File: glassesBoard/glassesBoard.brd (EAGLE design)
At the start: 87 x 27.6 mm, 26 parts, among them J1 AXK724147G, J2 105450-0101, U2 APDS-9960, U3 1.8, U4 3.3, U5 SSM3J338RSOT-23F, U6 SSM3J338RSOT-23F, U8 IQS263BDFN10

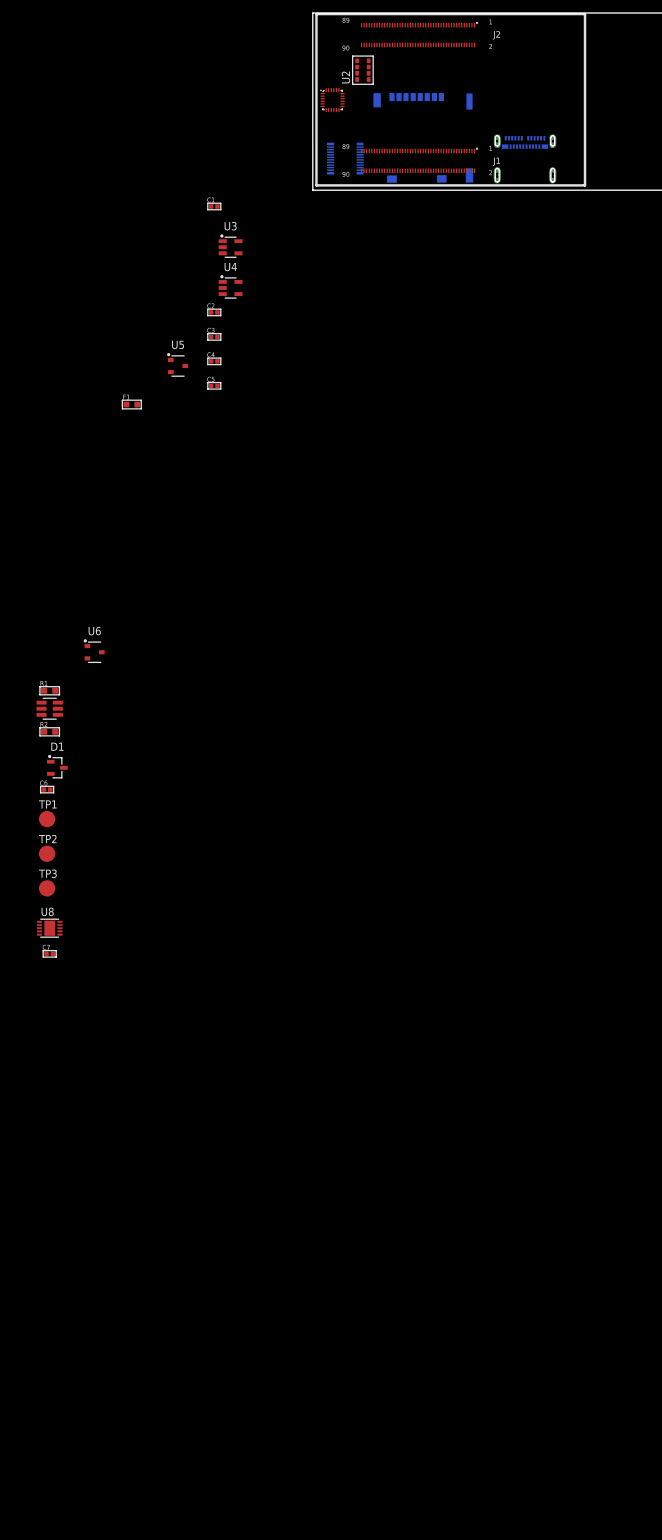
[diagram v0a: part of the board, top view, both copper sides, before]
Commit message: Added display converters and organized schematic
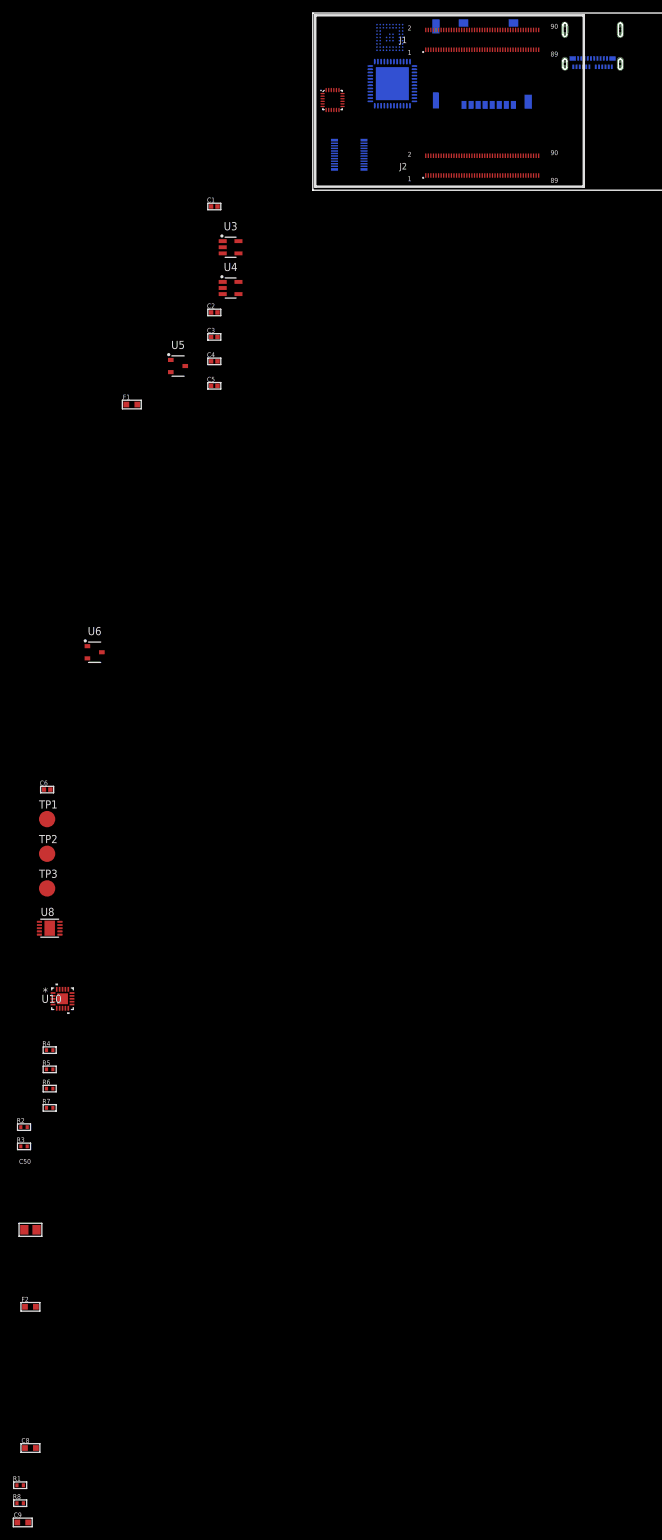
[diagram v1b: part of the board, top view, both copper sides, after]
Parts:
- removed C7: 1uF, thanics-capacitor:C0402
- removed D1: BAS40-06, glasses:SOT23-3
- removed J2: 105450-0101, 105450-0101:MOLEX_105450-0101
- removed U2: APDS-9960, glasses:APDS-9960
- added C50: 22uF, thanics-capacitor:C0805
- added C8, C9: 10uF, thanics-capacitor:C0603
- added F2: SF-0603S200-2, thanics-resistor:R0603
- added J7: 105450-0101, 105450-0101:MOLEX_105450-0101
- added R3: 10k, thanics-resistor:R0402
- added R4: 2.15k, thanics-resistor:R0402
- added R5: 1k, thanics-resistor:R0402
- added R6, R7: 3.2k, thanics-resistor:R0402
- added R8: 56k, thanics-resistor:R0402
- added U10: ATTINY20-MMH, attiny20:20M2
- added U11: SN65LVDS822VQFN48, glasses:QFN50P700X700X100-49T515
- R1: value 10k -> 56k; device 10k-resistor(0603):RC0603N-M -> thanics-resistor:R0402
- R2: device 10k-resistor(0603):RC0603N-M -> thanics-resistor:R0402
- U7: value (none) -> SN65DSI83PBGA-N64; device attiny10:6ST1-M -> glasses:BGA81C50P9X9_500X500X100
- moved R1 123.9 mm to (-36.6, -201.8)
- moved U7 117.3 mm to (21.0, 23.8), flipped to the bottom, turned to 270 degrees
- moved R2 61.7 mm to (-36.0, -146.0)
- moved U$1 22.6 mm to (35.4, 3.87), turned to 180 degrees
- moved U$2 12.4 mm to (37.0, 13.3), turned to 180 degrees
- moved J1 0.85 mm to (14.7, 5.52)
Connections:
- removed net FUSE_SNS: F1.2, R1.2, U6.2
- removed net N$6: C7.1, D1.3, R1.1, U6.1
- removed net SHIELD: J2.P$1, J2.P$2, J2.P$3, J2.P$4, J2.P$5, J2.P$6
- removed net VBUS: J2.A4, J2.A9, J2.B4, J2.B9
- new net !RST: R2.2, TP3.TP, U10.13
- new net !SHUTDOWN_INT: U10.2
- new net +5V: C6.1, C8.1, F2.2, R1.2, R2.1, R8.2, U10.9
- new net ADC: R5.1, R7.2, U10.5
- new net AIN1: R4.1, R6.2, U10.3
- new net FUSED_VBATT: C2.1, F1.2, R3.1, R4.2, R7.1, U3.1, U3.3, U6.2
- new net I2C_SCL_5V: U10.15
- new net I2C_SDA_5V/TPIDATA: TP2.TP, U10.12
- new net N$1: U11.26, U7.C8
- new net N$10: U11.33, U7.G9
- new net N$11: U11.32, U7.F8
- new net N$12: U11.31, U7.F9
- new net N$3: U11.25, U7.C9
- new net N$50: J7.A5, R8.1
- new net N$51: C50.1, F2.1, J7.A4, J7.A9, J7.B4, J7.B9
- new net N$63: J7.B5, R1.1
- new net N$8: U11.29, U7.E9
- new net N$9: U11.34, U7.G8
- new net TPICLK: TP1.TP, U10.11
- net !TOUCH_INT: no longer D1.1
- net +1V8: now also U10.4
- net +3V3: no longer R2.1, U7.5
- net BATT_CNTL: now also R3.2, U10.1, U6.1; no longer D1.2
- net GND: now also C50.2, C6.2, C8.2, J7.A1, J7.A12, J7.B1, J7.B12, J7.P$1, J7.P$2, J7.P$3, J7.P$4, J7.P$5, J7.P$6, R5.2, R6.1, U10.21, U10.8; no longer C7.2, J2.A1, J2.A12, J2.B1, J2.B12, U7.2
- net MIPI_DSI0_CLK_N: now also U7.J5
- net MIPI_DSI0_CLK_P: now also U7.H5
- net MIPI_DSI0_DATA0_N: now also U7.J3
- net MIPI_DSI0_DATA0_P: now also U7.H3
- net MIPI_DSI0_DATA1_N: now also U7.J4
- net MIPI_DSI0_DATA1_P: now also U7.H4
- net MIPI_DSI0_DATA2_N: now also U7.J6
- net MIPI_DSI0_DATA2_P: now also U7.H6
- net MIPI_DSI0_DATA3_N: now also U7.J7
- net MIPI_DSI0_DATA3_P: now also U7.H7
- net N$4: now also U11.28, U7.D8; no longer R2.2, TP1.TP, U7.6
- net N$5: now also U11.27, U7.D9; no longer TP3.TP, U7.3
- net N$7: now also U11.30, U7.E8; no longer TP2.TP, U7.1
- net P$1: no longer C2.1, U3.1, U3.3
- net USB_HS_D_N: now also J7.A7, J7.B7
- net USB_HS_D_P: now also J7.A6, J7.B6

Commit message: Added boot select circuitry
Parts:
- added C7: 22uF, thanics-capacitor:C0805
- added L1: 4.7uH, glasses:1008
- added R10, R11, R14, R15, R16, R9: 10k, thanics-resistor:R0402
- added R12, R13: 5.1k, thanics-resistor:R0603
- added U12: NLAS2750, glasses:UQFN10
- added U13, U15, U9: NX3020NAK, glasses:SOT-23_(TO-236AB)
- added U14: SSM3J338RSOT-23F, glasses:SOTFL95P240X80-3
- added U2: TPS613222A, glasses:SOT23-5
- C9: value 10uF -> 22uF; device thanics-capacitor:C0603 -> thanics-capacitor:C0805
- moved C9 18.4 mm to (-35.8, -226.0)
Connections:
- removed net MIPI_CSI0_CLK_N: U$1.J1.56
- removed net MIPI_CSI0_CLK_P: U$1.J1.58
- removed net MIPI_CSI0_DATA0_N: U$1.J1.64
- removed net MIPI_CSI0_DATA0_P: U$1.J1.66
- removed net MIPI_CSI0_DATA1_N: U$1.J1.60
- removed net MIPI_CSI0_DATA1_P: U$1.J1.62
- removed net MIPI_CSI0_DATA2_N: U$1.J1.48
- removed net MIPI_CSI0_DATA2_P: U$1.J1.50
- removed net MIPI_CSI0_DATA3_N: U$1.J1.52
- removed net MIPI_CSI0_DATA3_P: U$1.J1.54
- removed net N$50: J7.A5, R8.1
- removed net N$63: J7.B5, R1.1
- new net BOOT_CONFIG_0: U$1.J2.24
- new net BOOT_CONFIG_1: U$1.J2.22
- new net BOOT_CONFIG_2: U$1.J2.33
- new net BOOT_CONFIG_3: U$1.J2.26
- new net BOOT_CONFIG_5: R10.1, U$1.J2.35
- new net FORCED_USB_BOOT: U$1.J1.87
- new net I2C0_SCL: U$1.J1.79
- new net I2C0_SDA: U$1.J1.77
- new net I2C2_SCL: U$1.J1.88
- new net I2C2_SDA: U$1.J1.90
- new net I2C3_SCL: U$1.J2.67
- new net I2C3_SDA: U$1.J2.69
- new net MIPI_CSI1_CLK_N: U$1.J1.34
- new net MIPI_CSI1_CLK_P: U$1.J1.36
- new net MIPI_CSI1_DATA0_N: U$1.J1.42
- new net MIPI_CSI1_DATA0_P: U$1.J1.44
- new net MIPI_CSI1_DATA1_N: U$1.J1.38
- new net MIPI_CSI1_DATA1_P: U$1.J1.40
- new net N$13: U10.16, U9.G
- new net N$14: R11.1
- new net N$15: R14.1
- new net N$16: J7.B5, U12.9
- new net N$17: J7.A5, U12.3
- new net N$18: R13.2, U12.10
- new net N$19: R12.2, U12.2
- new net N$20: R1.1, U12.5
- new net N$21: R8.1, U12.7
- new net N$22: R15.2, U12.4, U12.8, U13.S
- new net N$23: R16.1, U14.1, U15.D
- new net N$6: L1.P$1, U2.1
- new net PHONE_ON_N: R9.1, U$1.J2.9, U9.D
- net +1V8: now also R10.2, R11.2, R14.2, R9.2
- net +5V: now also R16.2, U12.1, U13.D, U14.2, U2.4
- net AIN1: now also R6.1; no longer R6.2
- net FUSED_VBATT: now also L1.P$2
- net GND: now also C7.1, C9.2, R12.1, R13.1, R15.1, R6.2, U$1.J1.10, U$1.J1.31, U$1.J1.32, U$1.J1.37, U$1.J1.41, U$1.J1.45, U$1.J1.46, U$1.J1.47, U$1.J1.61, U$1.J1.68, U$1.J1.71, U$1.J1.78, U$1.J1.81, U$1.J1.86, U$1.J2.11, U$1.J2.15, U$1.J2.21, U$1.J2.30, U$1.J2.31, U$1.J2.36, U$1.J2.37, U$1.J2.42, U$1.J2.49, U$1.J2.5, U$1.J2.56, U$1.J2.65, U$1.J2.66, U$1.J2.77, U$1.J2.82, U$1.J2.89, U$1.J2.90, U12.6, U15.S, U2.2, U9.S; no longer R6.1
- net P$1: now also C7.2, C9.1, U$1.J1.1, U$1.J1.2, U$1.J1.3, U$1.J1.4, U$1.J1.5, U$1.J1.6, U$1.J1.7, U$1.J1.8
- net USB_HS_ID: now also U13.G, U15.G
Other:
- board text added: "Touch"

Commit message: Added charger, more boot settings, more power supplies, and fingerprint sensor
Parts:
- removed U$2: MICROSD, glasses:MICROSD
- added C10, C11, C12, C13, C14, C15, C16, C17, C21, C23: 1uF, thanics-capacitor:C0402
- added C18, C19, C20: 100nF, thanics-capacitor:C0402
- added C22: 10uF, thanics-capacitor:C0603
- added J2: DF30FC-30DS-0.4V, thanics-connector:DF30FC-30DS-0.4V
- added R17, R18, R19, R20, R23, R24, R25, R26, R27, R28: 10k, thanics-resistor:R0402
- added R21, R22: 5.1k, thanics-resistor:R0603
- added R29: 2k, thanics-resistor:R0402
- added U16: SSM3J338RSOT-23F, glasses:SOTFL95P240X80-3
- added U17: NX3020NAK, glasses:SOT-23_(TO-236AB)
- added U18: 2.8, glasses:SOT23-5
- added U19: TCR2EF15SOT-25, glasses:SOT95P275X130-5
- added U20: MICROSD, glasses:MICROSD
- added U21: MCP73833, glasses:DFN10-3X3
- J1: value AXK724147G -> BM10NB(0.8)-16DS-0.4V(51); device glasses:P4-24 -> thanics-connector:BM10NB(0.8)-16DS-0.4V(51)
- moved R14 122.0 mm to (-83.0, -359.4)
- moved J1 41.0 mm to (55.2, 12.0), flipped to the top, turned to 0 degrees
- moved U11 4.43 mm to (22.8, 12.4)
- moved U7 3.01 mm to (21.2, 20.8), turned to 180 degrees
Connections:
- new net !FINGER_RST: J1.10, R20.1, U$1.J1.75
- new net CAM1_PWDN: J2.12, U$1.J2.84
- new net CAM1_RST: J2.8, U$1.J1.82
- new net CAM1_XCLK: J2.23, U$1.J1.80
- new net CHARGER_VCC: C23.1, R17.2, U$1.J1.21, U14.3, U21.1, U21.2
- new net CHARGE_STAT1: R27.1, U$1.J2.48, U21.3
- new net CHARGE_STAT2: R28.1, U$1.J2.50, U21.4
- new net DSI_EN: C21.1, R25.2, U7.B1
- new net FINGER_INT: J1.8, U$1.J1.73
- new net N$24: F2.2, R16.2, R19.1, U14.2, U16.3
- new net N$25: R18.2, U16.1, U17.S
- new net N$26: R14.2, U7.A1, U7.H2
- new net N$27: R26.2, U21.8
- new net N$28: R29.2, U21.6
- new net N$29: C20.1, U1.10
- new net PM_RESIN_N: R24.1, U$1.J2.7
- new net SPI0_CLK: J1.16, U$1.J1.63
- new net SPI0_CS: J1.12, U$1.J1.67
- new net SPI0_MISO: J1.11, U$1.J1.69
- new net SPI0_MOSI: J1.15, U$1.J1.65
- net +1V8: now also C11.1, C13.1, C14.1, C17.1, C18.1, C19.1, J1.5, J1.7, J2.10, J2.2, J2.30, J2.6, R20.2, R21.2, R22.2, R24.2, R25.1, R27.2, R28.2, U1.13, U1.22, U1.8, U1.9, U18.5, U19.5, U7.A9, U7.B8, U7.D6, U7.E5, U7.E6, U7.F6, U7.J2; no longer R14.2
- net +3V3: now also C15.2, J1.6
- net +5V: now also U16.2, U17.D; no longer F2.2, R16.2, U14.2
- net GND: now also C10.2, C11.2, C12.2, C13.2, C14.2, C15.1, C16.2, C17.2, C18.2, C19.2, C20.2, C21.2, C22.2, C23.2, J1.13, J1.14, J1.3, J1.4, J1.9, J2.18, J2.21, J2.25, J2.26, J2.27, J2.29, J2.4, R14.1, R17.1, R18.1, R19.2, R23.1, R26.1, R29.1, U1.11, U1.18, U1.20, U18.2, U19.2, U20.10, U20.11, U20.12, U20.13, U20.6, U20.9, U21.5, U21.EXP, U7.A2, U7.A8, U7.B9, U7.D5, U7.E4, U7.F4, U7.F5, U7.H9; no longer U$2.10, U$2.11, U$2.12, U$2.13, U$2.6, U$2.9
- net I2C0_SCL: now also R22.1, U1.23
- net I2C0_SDA: now also R21.1, U1.24
- net I2C2_SCL: now also J2.14
- net I2C2_SDA: now also J2.16
- net I2C3_SCL: now also U7.H1
- net I2C3_SDA: now also U7.J1
- net MIPI_CSI1_CLK_N: now also J2.13
- net MIPI_CSI1_CLK_P: now also J2.15
- net MIPI_CSI1_DATA0_N: now also J2.9
- net MIPI_CSI1_DATA0_P: now also J2.11
- net MIPI_CSI1_DATA1_N: now also J2.17
- net MIPI_CSI1_DATA1_P: now also J2.19
- net N$15: now also C16.1, U7.J8; no longer R14.1
- net P$1: now also C10.1, C12.1, U$1.J1.11, U$1.J1.9, U18.1, U18.3, U19.1, U19.3
- net SDC2_CLK: now also U20.5; no longer U$2.5
- net SDC2_CMD: now also U20.3; no longer U$2.3
- net SDC2_DATA_0: now also U20.7; no longer U$2.7
- net SDC2_DATA_1: now also U20.8; no longer U$2.8
- net SDC2_DATA_2: now also U20.1; no longer U$2.1
- net SDC2_DATA_3: now also U20.2; no longer U$2.2
- net USB_HS_ID: now also R23.2, U17.G
- net VBATT_IN: now also C22.1, U21.10, U21.9
- net VREG_L11_SDC: now also U20.4; no longer U$2.4

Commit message: Started PCB component placement, made a premium service DRC
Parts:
- added C24: 1uF, thanics-capacitor:C0402
- added J3: S2B-XH-A(LF)(SN), thanics-connector:S2B-XH-A(LF)(SN)
- added R30, R31, R32, R33: 5.1k, thanics-resistor:R0402
- R12, R13, R21, R22: device thanics-resistor:R0603 -> thanics-resistor:R0402
- moved C22 421.6 mm to (82.3, 6.16)
- moved R29 421.6 mm to (78.8, 1.93)
- moved C23 420.3 mm to (75.3, 4.77), turned to 270 degrees
- moved R28 412.4 mm to (76.1, 1.67), turned to 270 degrees
- moved R26 412.2 mm to (81.8, 4.65), turned to 180 degrees
- moved R27 409.3 mm to (74.7, 1.67), turned to 270 degrees
- moved U21 407.3 mm to (78.3, 4.36)
- moved C21 403.2 mm to (13.9, 26.4), flipped to the bottom
- moved R25 399.3 mm to (13.9, 25.2), flipped to the bottom, turned to 180 degrees
- moved R14 395.5 mm to (13.9, 24.0), flipped to the bottom, turned to 180 degrees
- moved C17 391.0 mm to (14.3, 22.1), flipped to the bottom, turned to 90 degrees
- moved C16 389.5 mm to (21.9, 21.3), flipped to the bottom, turned to 180 degrees
- moved R23 387.0 mm to (51.5, 11.8), turned to 270 degrees
- moved R22 378.5 mm to (27.3, 19.6), flipped to the bottom, turned to 90 degrees
- moved R21 376.0 mm to (28.5, 19.6), flipped to the bottom, turned to 90 degrees
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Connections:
- new net !SHUTDOWN_LVDS: U11.37
- new net +1V5: C13.1, J2.6, U19.5
- new net +2V8: C11.1, J2.2, J2.30, U18.5
- net +1V8: now also R30.2, R31.2, R32.2, R33.2; no longer C11.1, C13.1, J2.2, J2.30, J2.6, U18.5, U19.5
- net +3V3: now also C24.1, U11.24, U11.44
- net GND: now also C24.2, J3.2, U11.36, U11.45, U11.49
- net I2C2_SCL: now also R30.1
- net I2C2_SDA: now also R31.1
- net I2C3_SCL: now also R33.1
- net I2C3_SDA: now also R32.1
- net VBATT_IN: now also J3.1
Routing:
- net MIPI_DSI0_DATA0_P: track 0.00 -> 15.5 mm, vias 0 -> 1
- net MIPI_DSI0_CLK_P: track 0.00 -> 14.6 mm, vias 0 -> 1
- net MIPI_DSI0_DATA0_N: track 0.00 -> 14.3 mm, vias 0 -> 1
- net MIPI_DSI0_CLK_N: track 0.00 -> 13.7 mm, vias 0 -> 1
- net MIPI_DSI0_DATA1_P: track 0.00 -> 13.4 mm, vias 0 -> 1
- net MIPI_DSI0_DATA2_P: track 0.00 -> 13.4 mm, vias 0 -> 1
- net MIPI_DSI0_DATA3_P: track 0.00 -> 13.3 mm, vias 0 -> 1
- net MIPI_DSI0_DATA3_N: track 0.00 -> 13.2 mm, vias 0 -> 1
- net MIPI_DSI0_DATA2_N: track 0.00 -> 12.9 mm, vias 0 -> 1
- net MIPI_DSI0_DATA1_N: track 0.00 -> 12.5 mm, vias 0 -> 1
- net N$1: track 0.00 -> 3.43 mm
- net N$9: track 0.00 -> 3.35 mm
- net N$4: track 0.00 -> 3.22 mm
- net N$11: track 0.00 -> 3.07 mm
- net N$7: track 0.00 -> 2.96 mm
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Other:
- board size 87 x 27.6 mm -> 82.9 x 28.4 mm
